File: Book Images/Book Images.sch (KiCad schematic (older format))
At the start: 6 parts, among them T1 Transformer

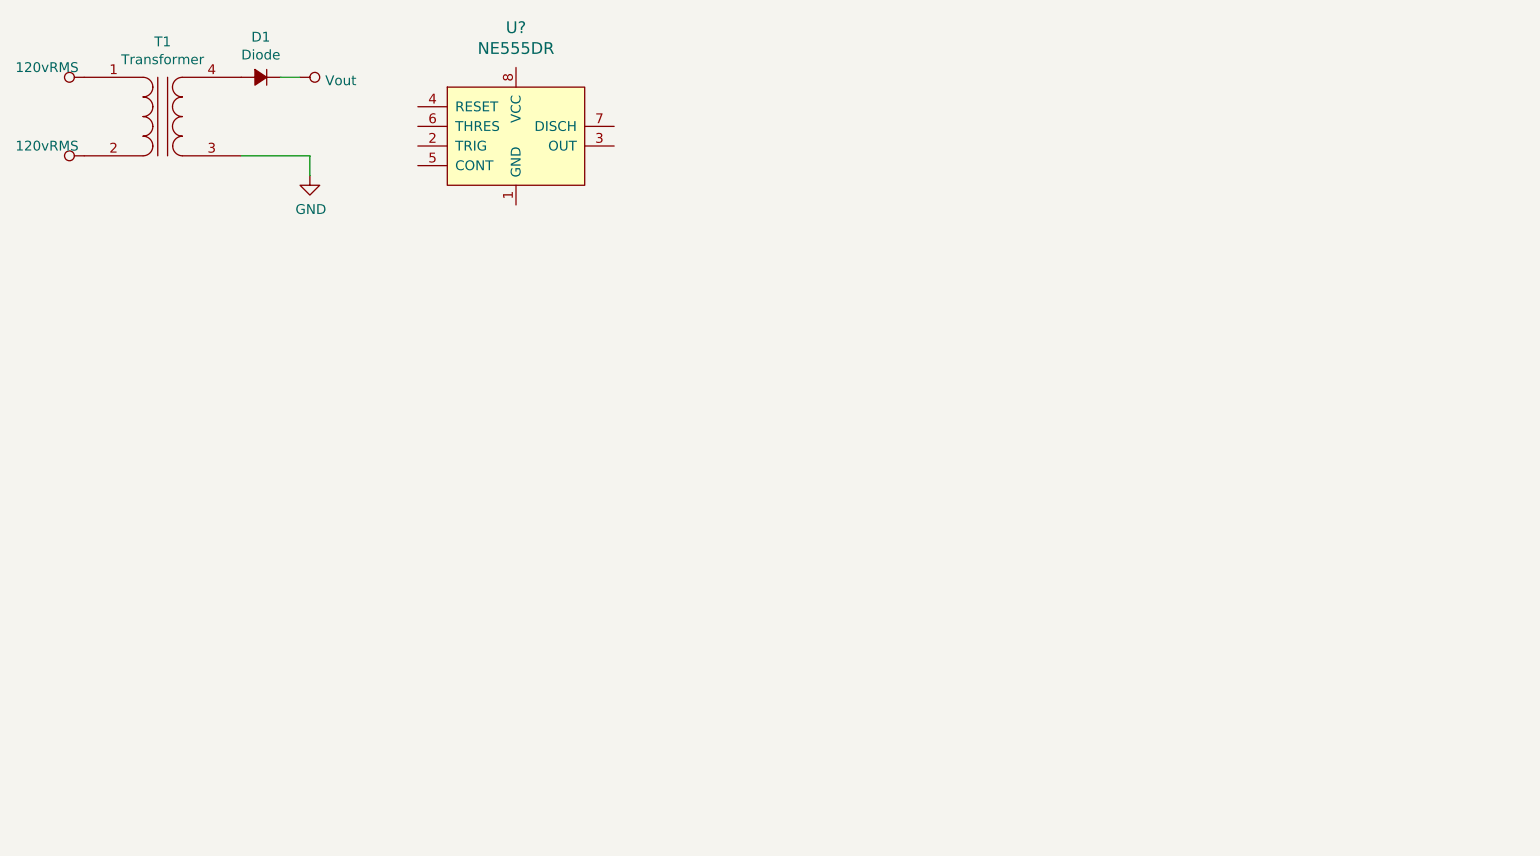
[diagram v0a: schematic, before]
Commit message: finished BJT regulators starting 7805
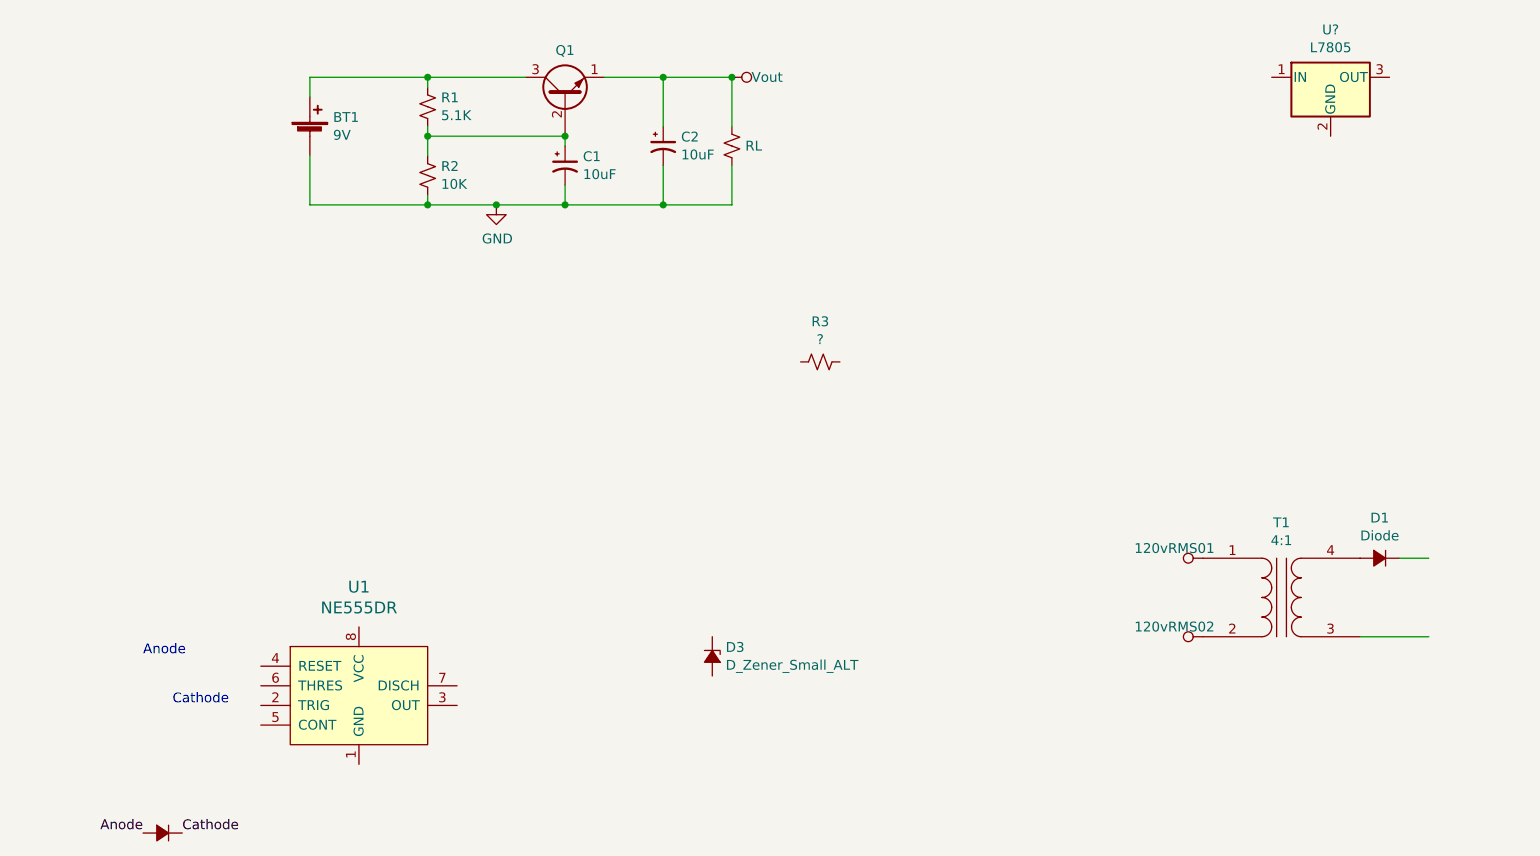
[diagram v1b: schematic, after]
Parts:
- added BT1: 9V, symbol Device:Battery_Cell
- added C1, C2: 10uF, symbol Device:CP1_Small
- added D2: Diode, symbol Device:D_Small_ALT
- added D3: D_Zener_Small_ALT, symbol Device:D_Zener_Small_ALT
- added Q1: 2N3904, Package_TO_SOT_THT:TO-92_Inline, symbol Transistor_BJT:2N3904
- added R1: 5.1K, symbol Device:R_Small_US
- added R2: 10K, symbol Device:R_Small_US
- added R3: ?, symbol Device:R_Small_US
- added RL: R_Small_US, symbol Device:R_Small_US
- added U?: L7805, symbol Regulator_Linear:L7805
- T1: value Transformer -> 4:1
- gave numbers to parts that had none: 1
- renumbered 120vRMS to 120vRMS01, 120vRMS to 120vRMS02
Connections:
- net labels added: Anode, Cathode
- wire segments 3 -> 24
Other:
- note added: "Anode"
- note added: "Cathode"
- moved on the sheet: D1, T1, U1

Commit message: updated corrections
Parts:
- BT1: value 9V -> 6V to 35V
- gave numbers to parts that had none: 1
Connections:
- wire segments 24 -> 36
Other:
- moved on the sheet: C1, C2, Q1, R1, R2, RL, U1
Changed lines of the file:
@@
 EESchema Schematic File Version 4
+LIBS:Book Images-cache
 EELAYER 30 0
 EELAYER END
@@
 L power:GND #PWR01
 U 1 1 62477070
-P 4300 2850
-F 0 "#PWR01" H 4300 2600 50  0001 C CNN
-F 1 "GND" H 4305 2677 50  0000 C CNN
-F 2 "" H 4300 2850 50  0001 C CNN
-F 3 "" H 4300 2850 50  0001 C CNN
-	1    4300 2850
+P 4200 2650
+F 0 "#PWR01" H 4200 2400 50  0001 C CNN
+F 1 "GND" H 4205 2477 50  0000 C CNN
+F 2 "" H 4200 2650 50  0001 C CNN
+F 3 "" H 4200 2650 50  0001 C CNN
+	1    4200 2650
 	1    0    0    -1
 $EndComp
@@
 L power:LINE Vout
 U 1 1 624789B6
-P 5500 2200
-F 0 "Vout" V 5500 2300 50  0000 L CNN
-F 1 "LINE" V 5517 2328 50  0001 L CNN
-F 2 "" H 5500 2200 50  0001 C CNN
-F 3 "" H 5500 2200 50  0001 C CNN
-	1    5500 2200
+P 5150 2200
+F 0 "Vout" V 5150 2300 50  0000 L CNN
+F 1 "LINE" V 5167 2328 50  0001 L CNN
+F 2 "" H 5150 2200 50  0001 C CNN
+F 3 "" H 5150 2200 50  0001 C CNN
+	1    5150 2200
 	0    1    1    0
 $EndComp
@@
 L Device:CP1_Small C1
 U 1 1 6279770B
-P 4650 2650
-F 0 "C1" H 4741 2696 50  0000 L CNN
-F 1 "10uF" H 4741 2605 50  0000 L CNN
-F 2 "" H 4650 2650 50  0001 C CNN
-F 3 "~" H 4650 2650 50  0001 C CNN
-	1    4650 2650
-	1    0    0    -1
-$EndComp
-Wire Wire Line
-	3350 2300 3350 2200
+P 3850 2450
+F 0 "C1" H 3941 2496 50  0000 L CNN
+F 1 "10uF" H 3941 2405 50  0000 L CNN
+F 2 "" H 3850 2450 50  0001 C CNN
+F 3 "~" H 3850 2450 50  0001 C CNN
+	1    3850 2450
+	1    0    0    -1
+$EndComp
 Wire Wire Line
 	8900 4650 9050 4650
@@
 L Transistor_BJT:2N3904 Q1
 U 1 1 627C06D4
-P 4650 2300
-F 0 "Q1" V 4887 2300 50  0000 C CNN
-F 1 "2N3904" H 4840 2255 50  0001 L CNN
-F 2 "Package_TO_SOT_THT:TO-92_Inline" H 4850 2225 50  0001 L CIN
-F 3 "https://www.fairchildsemi.com/datasheets/2N/2N3904.pdf" H 4650 2300 50  0001 L CNN
-	1    4650 2300
+P 8500 3100
+F 0 "Q1" V 8737 3100 50  0000 C CNN
+F 1 "2N3904" H 8690 3055 50  0001 L CNN
+F 2 "Package_TO_SOT_THT:TO-92_Inline" H 8700 3025 50  0001 L CIN
+F 3 "https://www.fairchildsemi.com/datasheets/2N/2N3904.pdf" H 8500 3100 50  0001 L CNN
+	1    8500 3100
 	0    -1   -1   0
 $EndComp
@@
 L Device:R_Small_US R1
 U 1 1 627C1712
-P 3950 2350
-F 0 "R1" H 4018 2396 50  0000 L CNN
-F 1 "5.1K" H 4018 2305 50  0000 L CNN
-F 2 "" H 3950 2350 50  0001 C CNN
-F 3 "~" H 3950 2350 50  0001 C CNN
-	1    3950 2350
+P 7800 3150
+F 0 "R1" H 7868 3196 50  0000 L CNN
+F 1 "5.1K" H 7868 3105 50  0000 L CNN
+F 2 "" H 7800 3150 50  0001 C CNN
+F 3 "~" H 7800 3150 50  0001 C CNN
+	1    7800 3150
 	1    0    0    -1
 $EndComp
@@
 L Device:R_Small_US R2
 U 1 1 627C39F3
-P 3950 2700
-F 0 "R2" H 4018 2746 50  0000 L CNN
-F 1 "10K" H 4018 2655 50  0000 L CNN
-F 2 "" H 3950 2700 50  0001 C CNN
-F 3 "~" H 3950 2700 50  0001 C CNN
-	1    3950 2700
+P 7800 3500
+F 0 "R2" H 7868 3546 50  0000 L CNN
+F 1 "10K" H 7868 3455 50  0000 L CNN
+F 2 "" H 7800 3500 50  0001 C CNN
+F 3 "~" H 7800 3500 50  0001 C CNN
+	1    7800 3500
 	1    0    0    -1
 $EndComp
@@
 L Device:R_Small_US RL
 U 1 1 627C7D77
-P 5500 2550
-F 0 "RL" H 5568 2550 50  0000 L CNN
-F 1 "R_Small_US" H 5568 2505 50  0001 L CNN
-F 2 "" H 5500 2550 50  0001 C CNN
-F 3 "~" H 5500 2550 50  0001 C CNN
-	1    5500 2550
+P 9350 3350
+F 0 "RL" H 9418 3350 50  0000 L CNN
+F 1 "R_Small_US" H 9418 3305 50  0001 L CNN
+F 2 "" H 9350 3350 50  0001 C CNN
+F 3 "~" H 9350 3350 50  0001 C CNN
+	1    9350 3350
 	1    0    0    -1
 $EndComp
@@
 L Device:CP1_Small C2
 U 1 1 627D3AA1
-P 5150 2550
-F 0 "C2" H 5241 2596 50  0000 L CNN
-F 1 "10uF" H 5241 2505 50  0000 L CNN
-F 2 "" H 5150 2550 50  0001 C CNN
-F 3 "~" H 5150 2550 50  0001 C CNN
-	1    5150 2550
-	1    0    0    -1
-$EndComp
-Wire Wire Line
-	4850 2200 5150 2200
-Wire Wire Line
-	3950 2850 4300 2850
-Wire Wire Line
-	3950 2850 3950 2800
-Wire Wire Line
-	4650 2850 5150 2850
-Wire Wire Line
-	5150 2200 5150 2450
-Wire Wire Line
-	5150 2650 5150 2850
-Wire Wire Line
-	3350 2200 3950 2200
-Wire Wire Line
-	3950 2250 3950 2200
-Connection ~ 3950 2200
-Wire Wire Line
-	3950 2850 3350 2850
-Connection ~ 3950 2850
-Wire Wire Line
-	3350 2600 3350 2850
+P 4900 2450
+F 0 "C2" H 4991 2496 50  0000 L CNN
+F 1 "10uF" H 4991 2405 50  0000 L CNN
+F 2 "" H 4900 2450 50  0001 C CNN
+F 3 "~" H 4900 2450 50  0001 C CNN
+	1    4900 2450
+	1    0    0    -1
+$EndComp
+Wire Wire Line
+	8700 3000 9000 3000
+Wire Wire Line
+	7800 3650 7800 3600
+Wire Wire Line
+	8500 3650 9000 3650
+Wire Wire Line
+	9000 3000 9000 3250
+Wire Wire Line
+	9000 3450 9000 3650
+Wire Wire Line
+	7200 3000 7800 3000
+Wire Wire Line
+	7800 3050 7800 3000
+Connection ~ 7800 3000
+Wire Wire Line
+	7800 3650 7200 3650
+Connection ~ 7800 3650
 $Comp
 L Device:Battery_Cell BT1
 U 1 1 627E13FD
 P 3350 2500
-F 0 "BT1" H 3468 2596 50  0000 L CNN
-F 1 "9V" H 3468 2505 50  0000 L CNN
+F 0 "BT1" H 3450 2550 50  0000 L CNN
+F 1 "6V to 35V" H 3350 2450 50  0000 L CNN
 F 2 "" V 3350 2560 50  0001 C CNN
 F 3 "~" V 3350 2560 50  0001 C CNN
@@
 $EndComp
 Wire Wire Line
-	3950 2450 3950 2500
-Wire Wire Line
-	3950 2200 4450 2200
-Wire Wire Line
-	4300 2850 4650 2850
-Connection ~ 4300 2850
-Connection ~ 4650 2850
-Wire Wire Line
-	4650 2500 4650 2550
-Wire Wire Line
-	4650 2750 4650 2850
-Wire Wire Line
-	4650 2500 3950 2500
-Connection ~ 4650 2500
-Connection ~ 3950 2500
-Wire Wire Line
-	3950 2500 3950 2600
-Wire Wire Line
-	5500 2450 5500 2200
-Wire Wire Line
-	5150 2200 5500 2200
-Connection ~ 5150 2200
-Connection ~ 5500 2200
-Wire Wire Line
-	5500 2650 5500 2850
-Wire Wire Line
-	5500 2850 5150 2850
-Connection ~ 5150 2850
-$Comp
-L Regulator_Linear:L7805 U?
+	7800 3250 7800 3300
+Wire Wire Line
+	7800 3000 8300 3000
+Connection ~ 8500 3650
+Wire Wire Line
+	8500 3300 8500 3350
+Wire Wire Line
+	8500 3550 8500 3650
+Wire Wire Line
+	8500 3300 7800 3300
+Connection ~ 8500 3300
+Connection ~ 7800 3300
+Wire Wire Line
+	7800 3300 7800 3400
+Wire Wire Line
+	9350 3250 9350 3000
+Wire Wire Line
+	9000 3000 9350 3000
+Connection ~ 9000 3000
+Wire Wire Line
+	9350 3450 9350 3650
+Wire Wire Line
+	9350 3650 9000 3650
+Connection ~ 9000 3650
+$Comp
+L Regulator_Linear:L7805 U1
 U 1 1 627EDF9E
-P 8550 2200
-F 0 "U?" H 8550 2442 50  0000 C CNN
-F 1 "L7805" H 8550 2351 50  0000 C CNN
-F 2 "" H 8575 2050 50  0001 L CIN
-F 3 "http://www.st.com/content/ccc/resource/technical/document/datasheet/41/4f/b3/b0/12/d4/47/88/CD00000444.pdf/files/CD00000444.pdf/jcr:content/translations/en.CD00000444.pdf" H 8550 2150 50  0001 C CNN
-	1    8550 2200
-	1    0    0    -1
-$EndComp
+P 4450 2200
+F 0 "U1" H 4450 2442 50  0000 C CNN
+F 1 "L7805" H 4450 2351 50  0000 C CNN
+F 2 "" H 4475 2050 50  0001 L CIN
+F 3 "http://www.st.com/content/ccc/resource/technical/document/datasheet/41/4f/b3/b0/12/d4/47/88/CD00000444.pdf/files/CD00000444.pdf/jcr:content/translations/en.CD00000444.pdf" H 4450 2150 50  0001 C CNN
+	1    4450 2200
+	1    0    0    -1
+$EndComp
+Wire Wire Line
+	4150 2200 3850 2200
+Wire Wire Line
+	3850 2200 3850 2350
+Connection ~ 3850 2200
+Wire Wire Line
+	3850 2200 3350 2200
+Wire Wire Line
+	4750 2200 4900 2200
+Wire Wire Line
+	4900 2650 4450 2650
+Wire Wire Line
+	3350 2650 3350 2600
+Wire Wire Line
+	3350 2300 3350 2200
+Wire Wire Line
+	3850 2550 3850 2650
+Connection ~ 3850 2650
+Wire Wire Line
+	3850 2650 3350 2650
+Wire Wire Line
+	4450 2500 4450 2650
+Connection ~ 4450 2650
+Wire Wire Line
+	4450 2650 4200 2650
+Wire Wire Line
+	5150 2200 4900 2200
+Connection ~ 4900 2200
+Connection ~ 4200 2650
+Wire Wire Line
+	4200 2650 3850 2650
+Wire Wire Line
+	7800 3650 8500 3650
+Wire Wire Line
+	4900 2200 4900 2350
+Wire Wire Line
+	4900 2550 4900 2650
 $EndSCHEMATC
